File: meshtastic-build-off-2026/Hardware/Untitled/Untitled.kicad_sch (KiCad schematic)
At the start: 0 parts

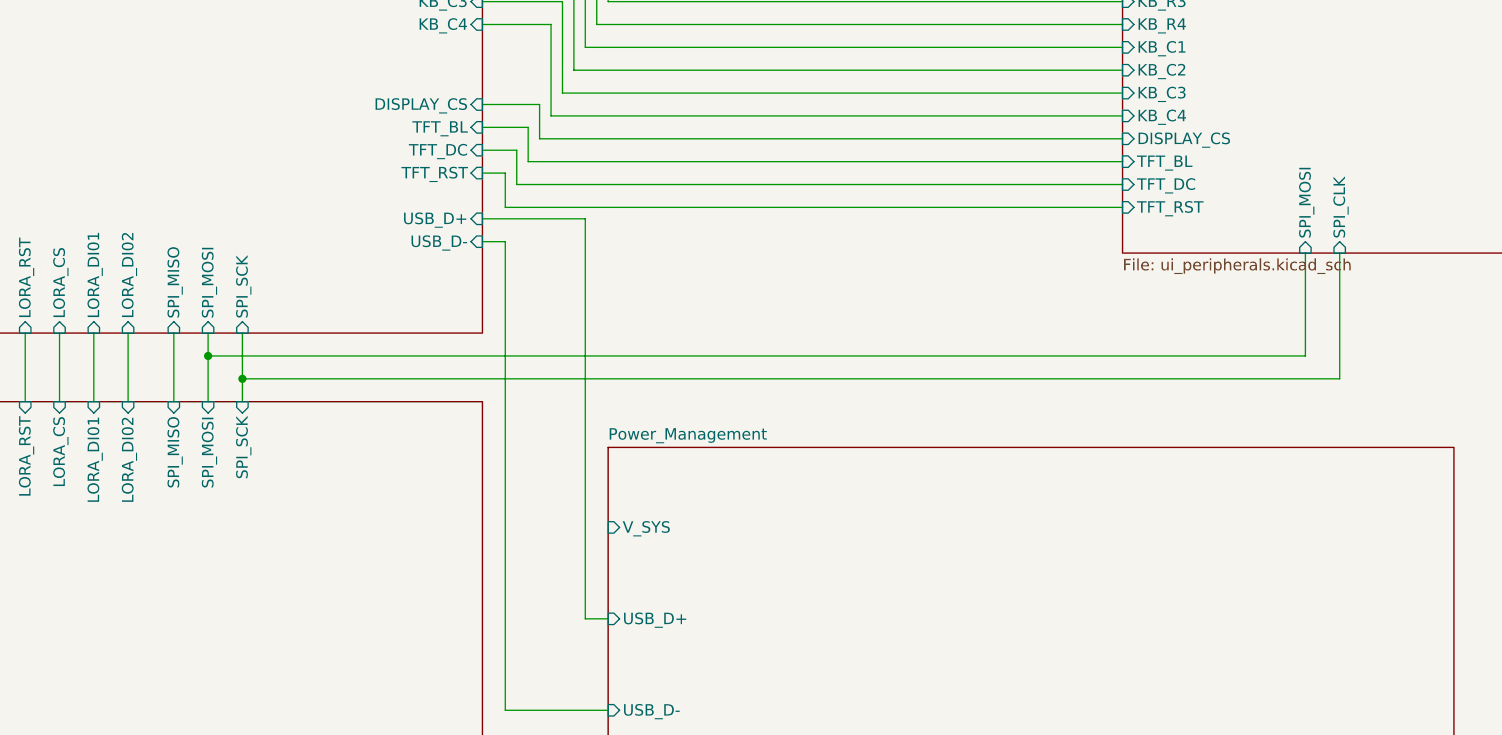
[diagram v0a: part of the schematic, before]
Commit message: Working DRC
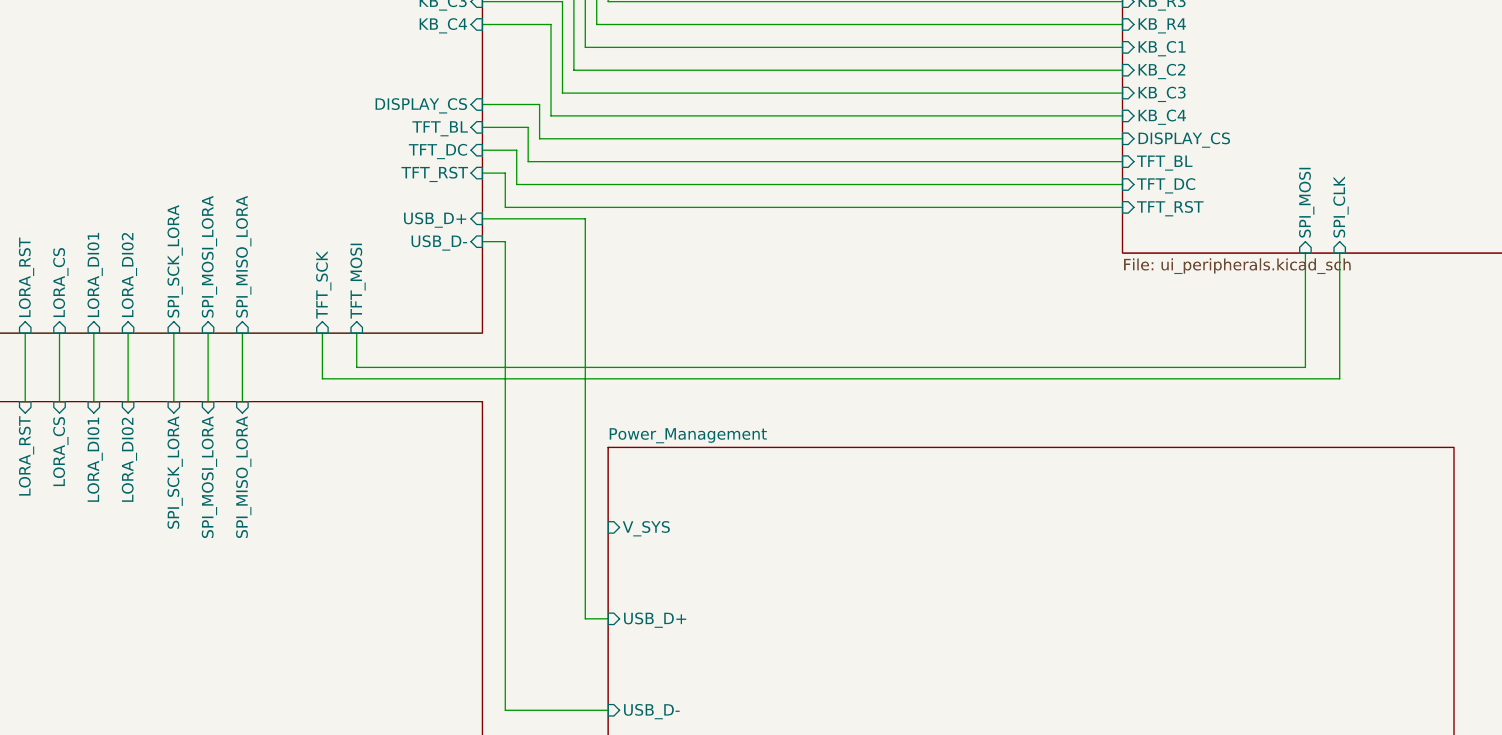
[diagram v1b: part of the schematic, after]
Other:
- sheet LoRa_Radio ports: added SPI_MISO_LORA, SPI_MOSI_LORA, SPI_SCK_LORA; removed SPI_MISO, SPI_MOSI, SPI_SCK
- sheet MCU_Core ports: added SPI_MISO_LORA, SPI_MOSI_LORA, SPI_SCK_LORA, TFT_MOSI, TFT_SCK; removed SPI_MISO, SPI_MOSI, SPI_SCK
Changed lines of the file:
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@@
 	(generator_version "9.0")
 	(paper "A4")
-	(junction
-		(at 71.12 73.66)
-		(diameter 0)
-		(color 0 0 0 0)
-	)
-	(junction
-		(at 74.93 76.2)
-		(diameter 0)
-		(color 0 0 0 0)
-	)
 	(wire
 		(pts
@@
 	(wire
 		(pts
-			(xy 74.93 71.12) (xy 74.93 76.2)
-		)
-		(stroke
-			(width 0)
-			(type default)
-		)
-	)
-	(wire
-		(pts
-			(xy 71.12 73.66) (xy 71.12 78.74)
+			(xy 71.12 71.12) (xy 71.12 78.74)
 		)
 		(stroke
@@
 	(wire
 		(pts
+			(xy 83.82 71.12) (xy 83.82 76.2)
+		)
+		(stroke
+			(width 0)
+			(type default)
+		)
+	)
+	(wire
+		(pts
 			(xy 101.6 58.42) (xy 113.03 58.42)
 		)
@@
 	(wire
 		(pts
-			(xy 193.04 73.66) (xy 193.04 62.23)
-		)
-		(stroke
-			(width 0)
-			(type default)
-		)
-	)
-	(wire
-		(pts
 			(xy 109.22 36.83) (xy 101.6 36.83)
 		)
@@
 	(wire
 		(pts
-			(xy 74.93 76.2) (xy 196.85 76.2)
+			(xy 83.82 76.2) (xy 196.85 76.2)
 		)
 		(stroke
@@
 	(wire
 		(pts
+			(xy 87.63 71.12) (xy 87.63 74.93)
+		)
+		(stroke
+			(width 0)
+			(type default)
+		)
+	)
+	(wire
+		(pts
 			(xy 115.57 34.29) (xy 172.72 34.29)
 		)
@@
 	(wire
 		(pts
-			(xy 71.12 73.66) (xy 193.04 73.66)
-		)
-		(stroke
-			(width 0)
-			(type default)
-		)
-	)
-	(wire
-		(pts
 			(xy 116.84 21.59) (xy 101.6 21.59)
 		)
@@
 	(wire
 		(pts
+			(xy 87.63 74.93) (xy 193.04 74.93)
+		)
+		(stroke
+			(width 0)
+			(type default)
+		)
+	)
+	(wire
+		(pts
 			(xy 113.03 29.21) (xy 101.6 29.21)
 		)
@@
 	(wire
 		(pts
-			(xy 74.93 76.2) (xy 74.93 78.74)
+			(xy 74.93 71.12) (xy 74.93 78.74)
 		)
 		(stroke
@@
 	(wire
 		(pts
-			(xy 71.12 71.12) (xy 71.12 73.66)
-		)
-		(stroke
-			(width 0)
-			(type default)
-		)
-	)
-	(wire
-		(pts
 			(xy 113.03 58.42) (xy 113.03 102.87)
+		)
+		(stroke
+			(width 0)
+			(type default)
+		)
+	)
+	(wire
+		(pts
+			(xy 193.04 62.23) (xy 193.04 74.93)
 		)
 		(stroke
@@
 			)
 		)
-		(pin "SPI_MOSI" input
-			(at 71.12 78.74 90)
-			(effects
-				(font
-					(size 1.27 1.27)
-				)
-				(justify right)
-			)
-		)
-		(pin "SPI_SCK" input
-			(at 74.93 78.74 90)
-			(effects
-				(font
-					(size 1.27 1.27)
-				)
-				(justify right)
-			)
-		)
-		(pin "SPI_MISO" input
-			(at 67.31 78.74 90)
-			(effects
-				(font
-					(size 1.27 1.27)
-				)
-				(justify right)
-			)
-		)
 		(pin "LORA_CS" input
 			(at 54.61 78.74 90)
@@
 		(pin "LORA_DI01" input
 			(at 58.42 78.74 90)
+			(effects
+				(font
+					(size 1.27 1.27)
+				)
+				(justify right)
+			)
+		)
+		(pin "SPI_MOSI_LORA" input
+			(at 71.12 78.74 90)
+			(effects
+				(font
+					(size 1.27 1.27)
+				)
+				(justify right)
+			)
+		)
+		(pin "SPI_SCK_LORA" input
+			(at 67.31 78.74 90)
+			(effects
+				(font
+					(size 1.27 1.27)
+				)
+				(justify right)
+			)
+		)
+		(pin "SPI_MISO_LORA" input
+			(at 74.93 78.74 90)
 			(effects
 				(font
@@
 			)
 		)
-		(pin "SPI_MISO" input
-			(at 67.31 71.12 270)
-			(effects
-				(font
-					(size 1.27 1.27)
-				)
-				(justify left)
-			)
-		)
-		(pin "SPI_MOSI" input
-			(at 71.12 71.12 270)
-			(effects
-				(font
-					(size 1.27 1.27)
-				)
-				(justify left)
-			)
-		)
 		(pin "KB_R3" input
 			(at 101.6 24.13 0)
@@
 			)
 		)
-		(pin "SPI_SCK" input
+		(pin "TFT_MOSI" input
+			(at 87.63 71.12 270)
+			(effects
+				(font
+					(size 1.27 1.27)
+				)
+				(justify left)
+			)
+		)
+		(pin "TFT_SCK" input
+			(at 83.82 71.12 270)
+			(effects
+				(font
+					(size 1.27 1.27)
+				)
+				(justify left)
+			)
+		)
+		(pin "SPI_SCK_LORA" input
+			(at 67.31 71.12 270)
+			(effects
+				(font
+					(size 1.27 1.27)
+				)
+				(justify left)
+			)
+		)
+		(pin "SPI_MOSI_LORA" input
+			(at 71.12 71.12 270)
+			(effects
+				(font
+					(size 1.27 1.27)
+				)
+				(justify left)
+			)
+		)
+		(pin "SPI_MISO_LORA" input
 			(at 74.93 71.12 270)
 			(effects
